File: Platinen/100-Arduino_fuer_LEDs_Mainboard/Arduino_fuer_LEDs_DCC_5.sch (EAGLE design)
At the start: 115 parts, among them IC1 7805, IC2 LM393N, J1 Tag/Nacht, U1 WS2812_MODUL, U2 LED NANO, U3 DCC NANO, U4 WS2812_MODUL, X1 RJ10, X2 AK500/2+M, X3 MAB 5SH Conrad: 738247 - VQ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

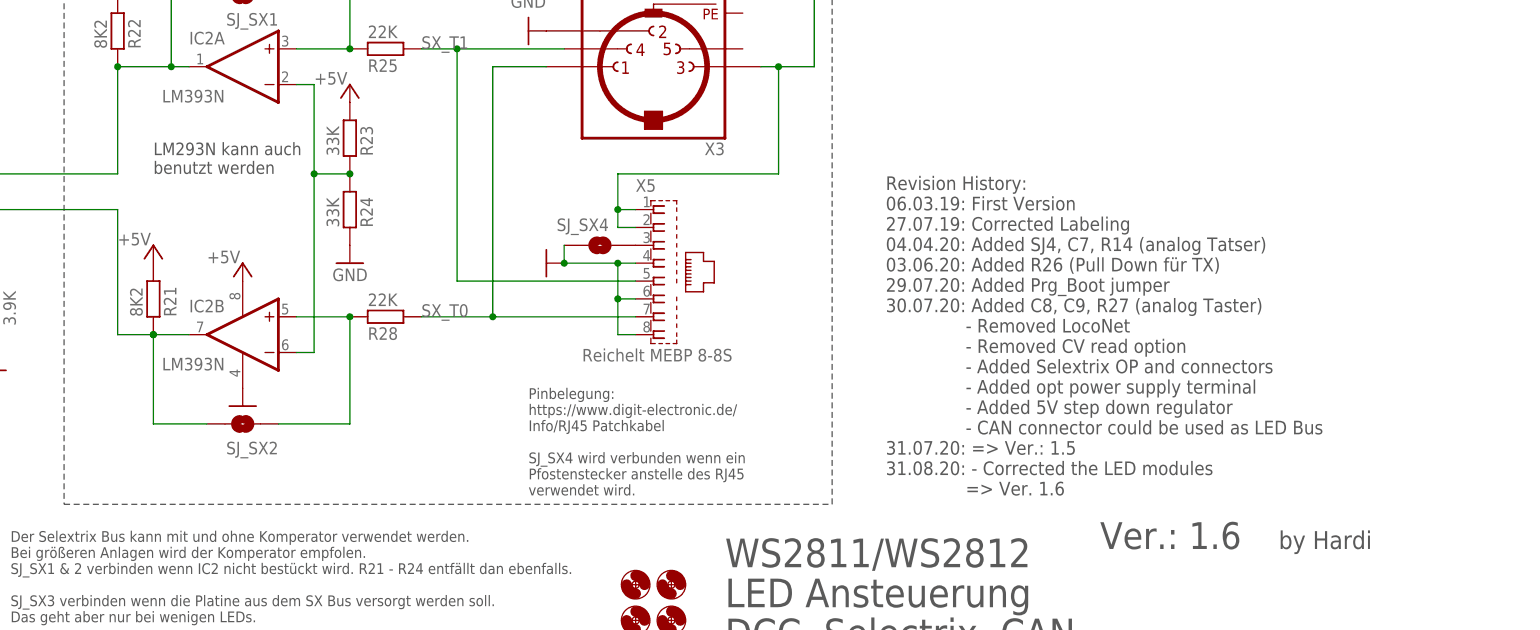
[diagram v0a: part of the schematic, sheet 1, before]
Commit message: Changed LM293 comment
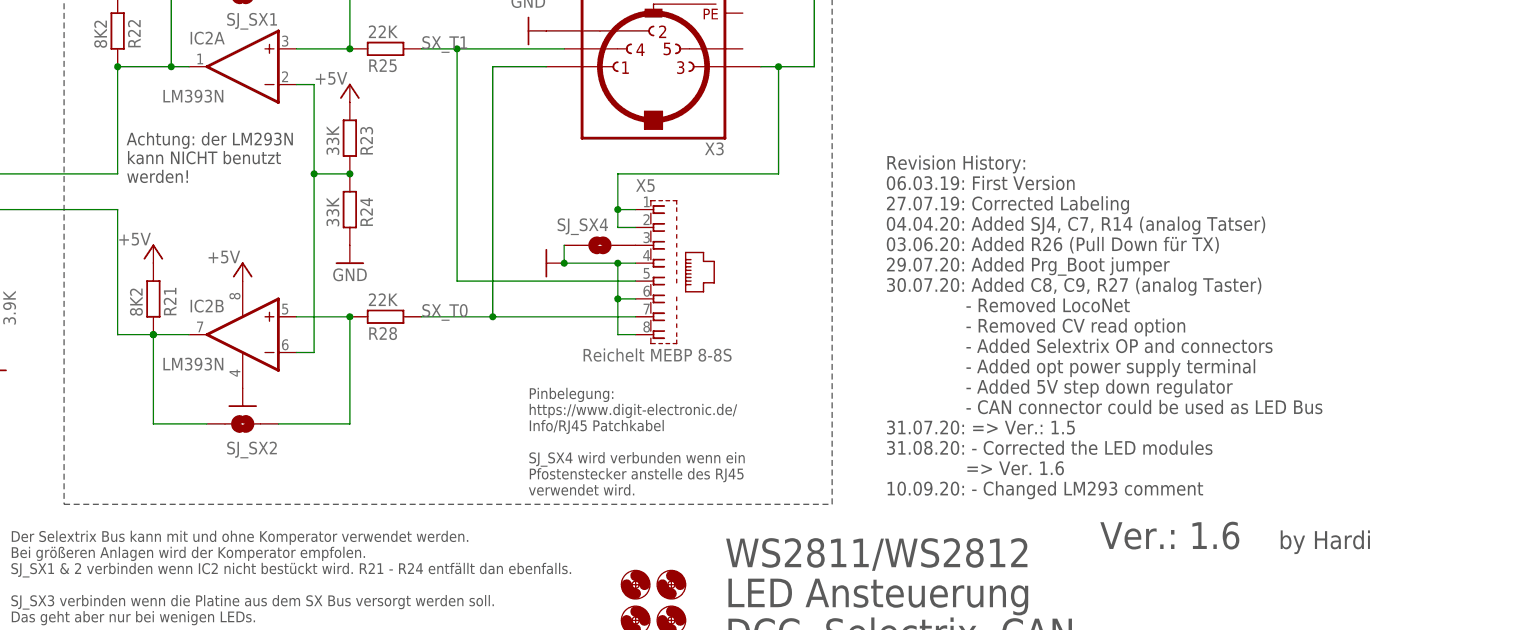
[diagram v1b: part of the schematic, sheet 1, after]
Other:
- note added: "Achtung: der LM293N kann NICHT benutzt werden!"
- note removed: "LM293N kann auch benutzt werden"
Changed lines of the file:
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@@
 31.07.20: =&gt; Ver.: 1.5
 31.08.20: - Corrected the LED modules
-               =&gt; Ver. 1.6</text>
+               =&gt; Ver. 1.6
+10.09.20: - Changed LM293 comment</text>
 <text x="-91.44" y="31.75" size="1.778" layer="91">O2</text>
 <text x="-91.44" y="16.51" size="1.778" layer="91">O1</text>
@@
 dann kann OK1 entfallen. Stattdessen wird eine Diode Pin3 nach Pin2
 verwendet und NO_OPTO verbunden.</text>
-<text x="104.14" y="38.1" size="1.778" layer="97">LM293N kann auch
-benutzt werden</text>
+<text x="100.33" y="36.83" size="1.778" layer="97">Achtung: der LM293N
+kann NICHT benutzt
+werden!</text>
 </plain>
 <instances>
